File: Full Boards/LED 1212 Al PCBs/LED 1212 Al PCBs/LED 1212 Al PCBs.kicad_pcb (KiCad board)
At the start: 2 copper layers, 25 x 26.5 mm, 4 parts

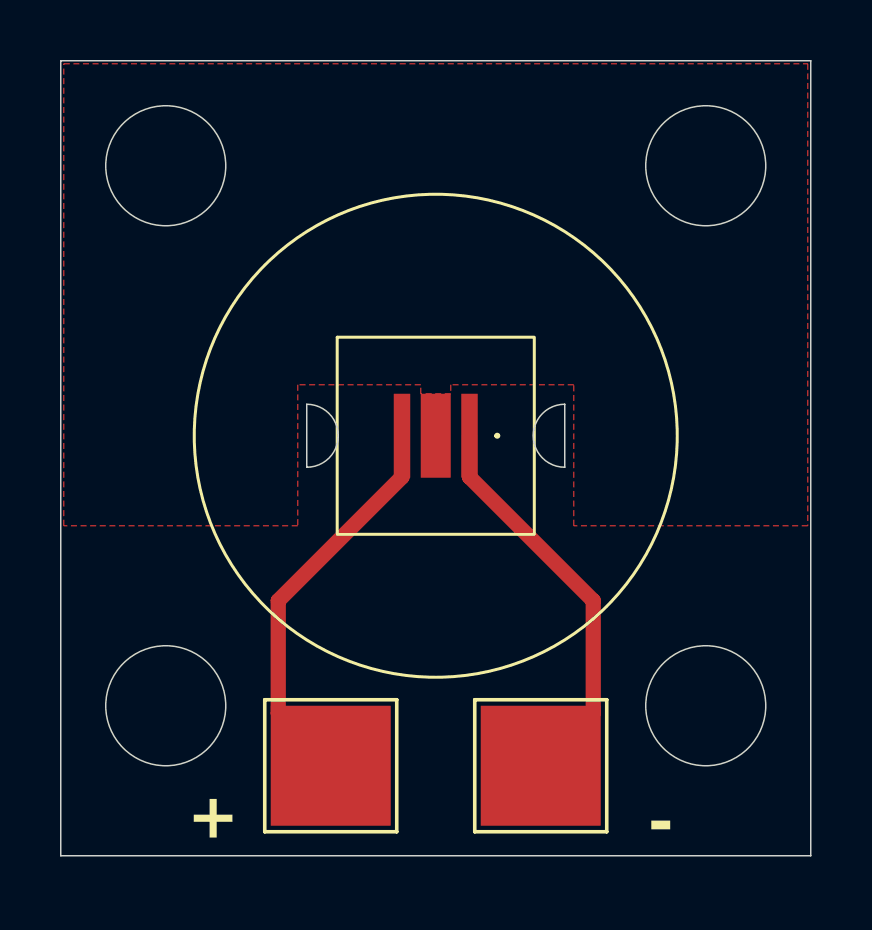
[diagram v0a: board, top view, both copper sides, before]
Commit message: Updated / resized the key holes for the lenses.
Signed-off-by: digimer <digital.mermaid@gmail.com>
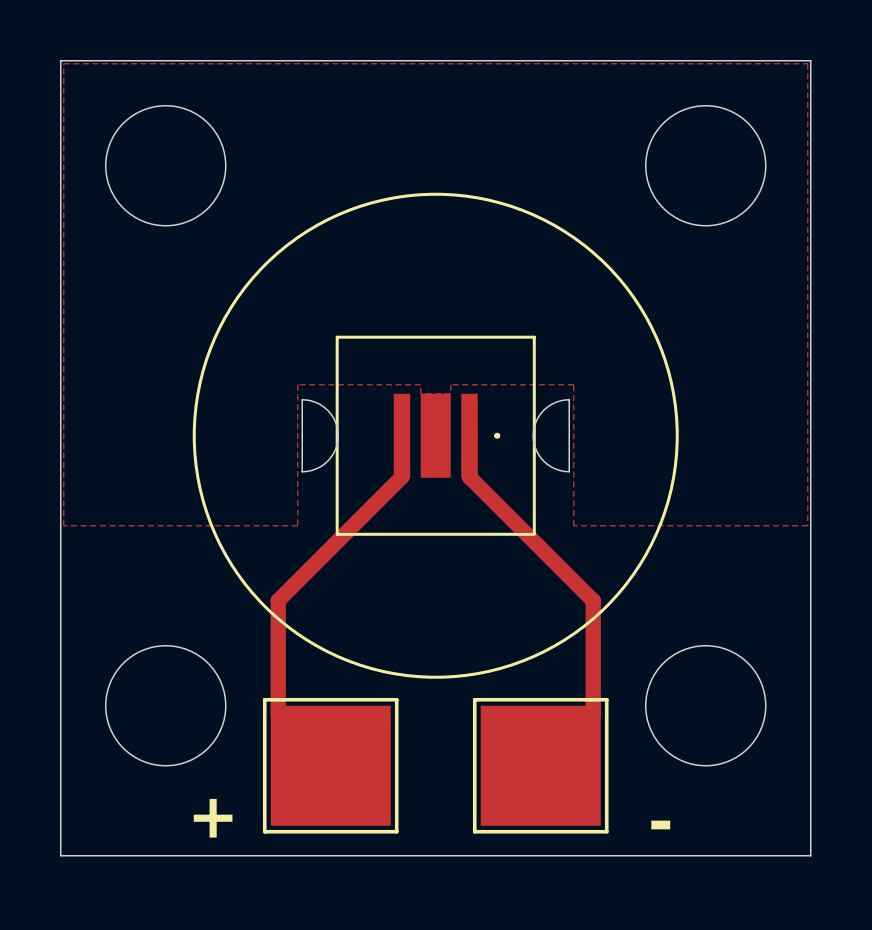
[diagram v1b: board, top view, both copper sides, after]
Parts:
- removed REF**: LEDiL TINA-Y, mr-stuff:LEDiL TINA-Y
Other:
- outline, holes or cut-outs redrawn
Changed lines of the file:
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@@
 	)
 	(paper "A4")
+	(title_block
+		(date "2026-08-07")
+		(rev "v1.1")
+	)
 	(layers
 		(0 "F.Cu" signal)
@@
 		(capping no)
 		(filling no)
-		(zone_defaults)
 		(pcbplotparams
 			(layerselection 0x00000000_00000000_55555555_5755f5ff)
@@
 		(embedded_fonts no)
 	)
-	(footprint "mr-stuff:LEDiL TINA-Y"
-		(layer "F.Cu")
-		(at 100 100)
-		(property "Reference" "REF**"
-			(at 0 -9.25 0)
-			(unlocked yes)
-			(layer "F.SilkS")
-			(hide yes)
-			(effects
-				(font
-					(size 1 1)
-					(thickness 0.1)
-				)
-			)
-		)
-		(property "Value" "LEDiL TINA-Y"
-			(at 0 -9.25 0)
-			(unlocked yes)
-			(layer "F.Fab")
-			(hide yes)
-			(effects
-				(font
-					(size 1 1)
-					(thickness 0.15)
-				)
-			)
-		)
-		(property "Datasheet" ""
-			(at 0 0 0)
-			(unlocked yes)
-			(layer "F.Fab")
-			(hide yes)
-			(effects
-				(font
-					(size 1 1)
-					(thickness 0.15)
-				)
-			)
-		)
-		(property "Description" ""
-			(at 0 0 0)
-			(unlocked yes)
-			(layer "F.Fab")
-			(hide yes)
-			(effects
-				(font
-					(size 1 1)
-					(thickness 0.15)
-				)
-			)
-		)
-		(attr board_only exclude_from_pos_files exclude_from_bom)
-		(duplicate_pad_numbers_are_jumpers no)
-		(fp_rect
-			(start -3.285 -3.285)
-			(end 3.285 3.285)
-			(stroke
-				(width 0.1)
-				(type solid)
-			)
-			(fill no)
-			(layer "F.SilkS")
-		)
-		(fp_circle
-			(center 0 0)
-			(end 8.05 0)
-			(stroke
-				(width 0.1)
-				(type solid)
-			)
-			(fill no)
-			(layer "F.SilkS")
-		)
-		(fp_line
-			(start -4.3 -1.05)
-			(end -4.3 1.05)
-			(stroke
-				(width 0.05)
-				(type default)
-			)
-			(layer "Edge.Cuts")
-		)
-		(fp_line
-			(start 4.3 1.05)
-			(end 4.3 -1.05)
-			(stroke
-				(width 0.05)
-				(type default)
-			)
-			(layer "Edge.Cuts")
-		)
-		(fp_arc
-			(start -4.3 -1.05)
-			(mid -3.25 0)
-			(end -4.3 1.05)
-			(stroke
-				(width 0.05)
-				(type default)
-			)
-			(layer "Edge.Cuts")
-		)
-		(fp_arc
-			(start 4.3 1.05)
-			(mid 3.25 0)
-			(end 4.3 -1.05)
-			(stroke
-				(width 0.05)
-				(type default)
-			)
-			(layer "Edge.Cuts")
-		)
-		(fp_text user "${REFERENCE}"
-			(at 0 -9.25 0)
-			(unlocked yes)
-			(layer "F.Fab")
-			(effects
-				(font
-					(size 1 1)
-					(thickness 0.15)
-				)
-			)
-		)
-		(embedded_fonts no)
-		(model "${MY_3DMODELS}/LEDiL TINA-Y/LEDiL_TINA-Y-WHT.step"
-			(hide yes)
-			(offset
-				(xyz 0 0 0)
-			)
-			(scale
-				(xyz 1 1 1)
-			)
-			(rotate
-				(xyz -0 -0 -0)
-			)
-		)
-	)
 	(footprint "TestPoint:TestPoint_Pad_4.0x4.0mm"
 		(layer "F.Cu")
@@
 	)
 	(gr_rect
+		(start 96.715 96.715)
+		(end 103.285 103.285)
+		(stroke
+			(width 0.1)
+			(type default)
+		)
+		(fill no)
+		(layer "F.SilkS")
+	)
+	(gr_circle
+		(center 100 100)
+		(end 108.05 100)
+		(stroke
+			(width 0.1)
+			(type default)
+		)
+		(fill no)
+		(layer "F.SilkS")
+	)
+	(gr_rect
 		(start 87.5 87.5)
 		(end 112.5 114)
@@
 		(layer "Edge.Cuts")
 	)
+	(gr_line
+		(start 95.55 98.8)
+		(end 95.55 101.2)
+		(stroke
+			(width 0.05)
+			(type default)
+		)
+		(layer "Edge.Cuts")
+	)
+	(gr_arc
+		(start 95.55 98.8)
+		(mid 96.75 100)
+		(end 95.55 101.2)
+		(stroke
+			(width 0.05)
+			(type solid)
+		)
+		(layer "Edge.Cuts")
+	)
+	(gr_line
+		(start 104.45 101.2)
+		(end 104.45 98.8)
+		(stroke
+			(width 0.05)
+			(type default)
+		)
+		(layer "Edge.Cuts")
+	)
+	(gr_arc
+		(start 104.45 101.2)
+		(mid 103.25 100)
+		(end 104.45 98.8)
+		(stroke
+			(width 0.05)
+			(type solid)
+		)
+		(layer "Edge.Cuts")
+	)
